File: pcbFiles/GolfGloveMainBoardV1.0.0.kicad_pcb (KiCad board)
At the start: 2 copper layers, 10.5 x 14 mm, 79 parts, among them J1 USB_C_Receptacle, J10 A-1JB, J11 Conn_01x16_Male, J12 HOST_WAKE, J13 TP4, J14 Conn_01x02_Male, J15 Conn_01x02_Male, J2 BT_UART, J3 USB_C_Receptacle, J4 Conn_01x01, J5 Conn_01x01, J6 Conn_01x02_Male, J7 Conn_01x02_Male, J8 Conn_01x02_Male, J9 Conn_01x02_Male, SW1 SW_SPDT, SW2 SW_Push, U1 LSM9DS1TR, U2 LSM9DS1TR, U3 TPS63001DRCT, U4 CYW20719B1KUMLG, U5 MCP73831T-2ACI/OT, U6 XC6119N16A7R-G, Y1 Crystal, Y2 Crystal_GND23

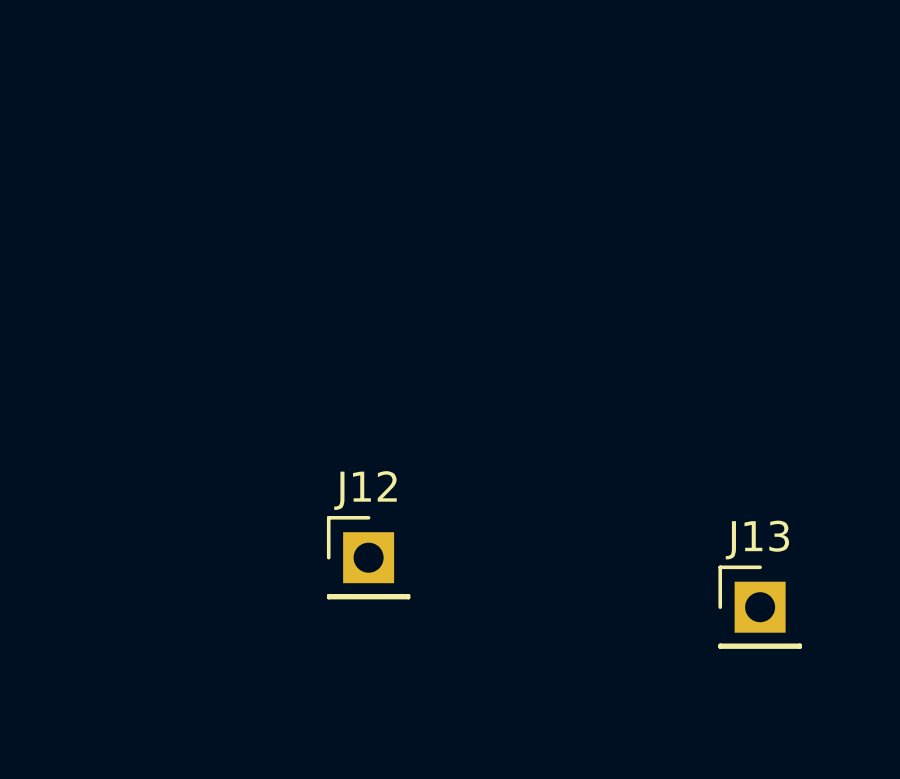
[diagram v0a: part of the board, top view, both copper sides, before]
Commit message: Update Footprints and Board Layers
Still need to get foorprint for x... device and the lpf may need to make them if I cannot find them @willcarroll7
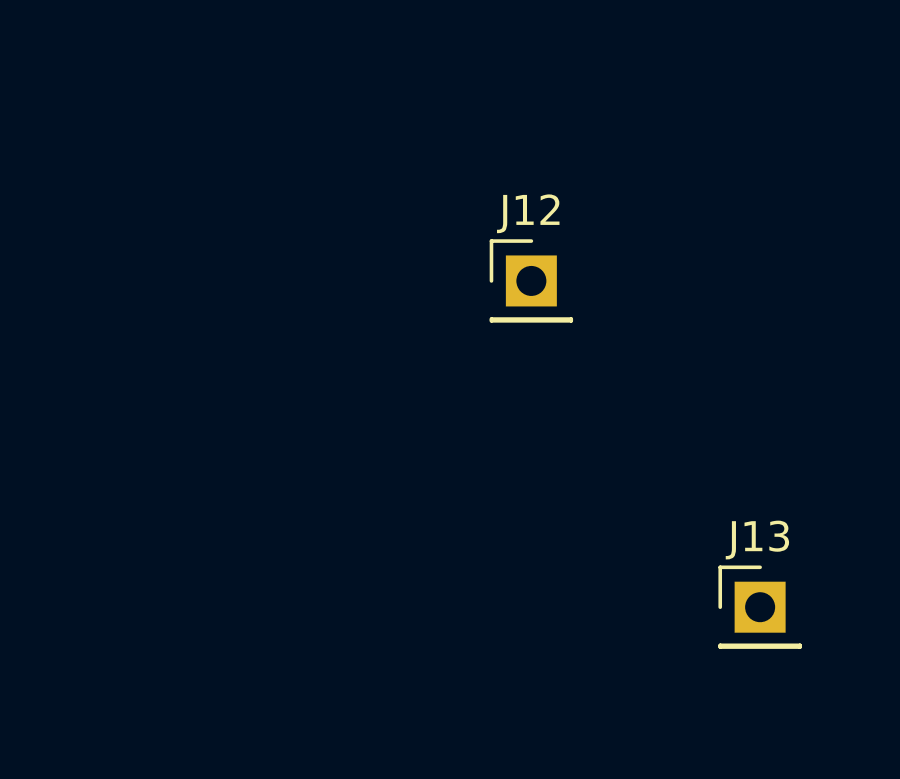
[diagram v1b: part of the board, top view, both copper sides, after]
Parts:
- moved J12 10.7 mm to (168.1, 56.0)
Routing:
- net Net-(J12-Pad1): track 0.00 -> 1.41 mm
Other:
- copper layers 2 -> 4
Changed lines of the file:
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@@
     (thickness 1.6)
     (drawings 11)
-    (tracks 139)
+    (tracks 141)
     (zones 0)
     (modules 79)
@@
   (layers
     (0 F.Cu signal)
+    (1 In1.Cu signal)
+    (2 In2.Cu signal)
     (31 B.Cu signal)
     (32 B.Adhes user)
@@
     (last_trace_width 0.25)
     (trace_clearance 0.15)
-    (zone_clearance 0.508)
+    (zone_clearance 0.25)
     (zone_45_only no)
     (trace_min 0.2)
@@
   )
   (module Pin_Headers:Pin_Header_Straight_1x01_Pitch2.54mm (layer F.Cu)
-    (at 162.7 65.25)
+    (at 168.125 56.025)
     (descr "Through hole straight pin header, 1x01, 2.54mm pitch, single row")
     (tags "Through hole pin header THT 1x01 2.54mm single row")
@@
   (segment (start 68.99 58.365) (end 68.7 58.175) (width 0.25) (layer F.Cu) (net 57))
   (segment (start 71.65 54.125) (end 71.65 53.81) (width 0.25) (layer B.Cu) (net 57))
+  (segment (start 168.125 56.025) (end 168.25 55.9) (width 0.25) (layer B.Cu) (net 88))
+  (segment (start 168.125 56.025) (end 169 55.15) (width 0.25) (layer In1.Cu) (net 88))
 )

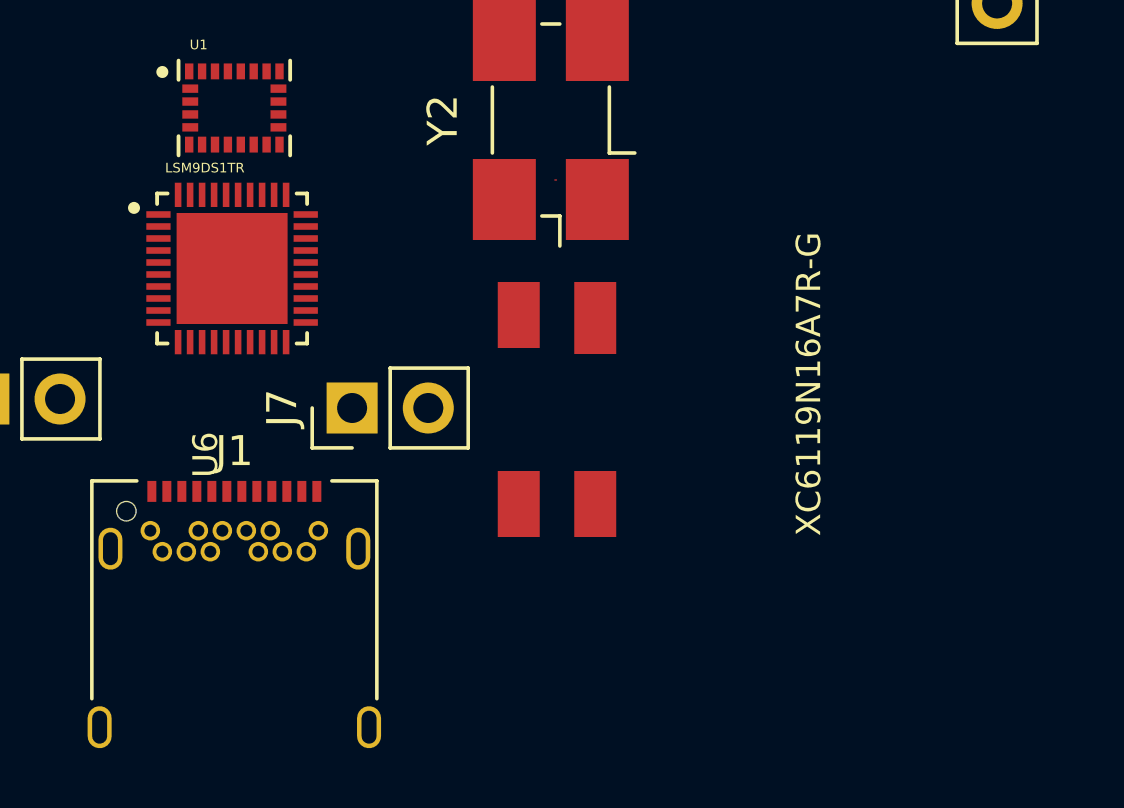
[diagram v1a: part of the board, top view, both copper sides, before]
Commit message: Update the Voltage Detector Footprint
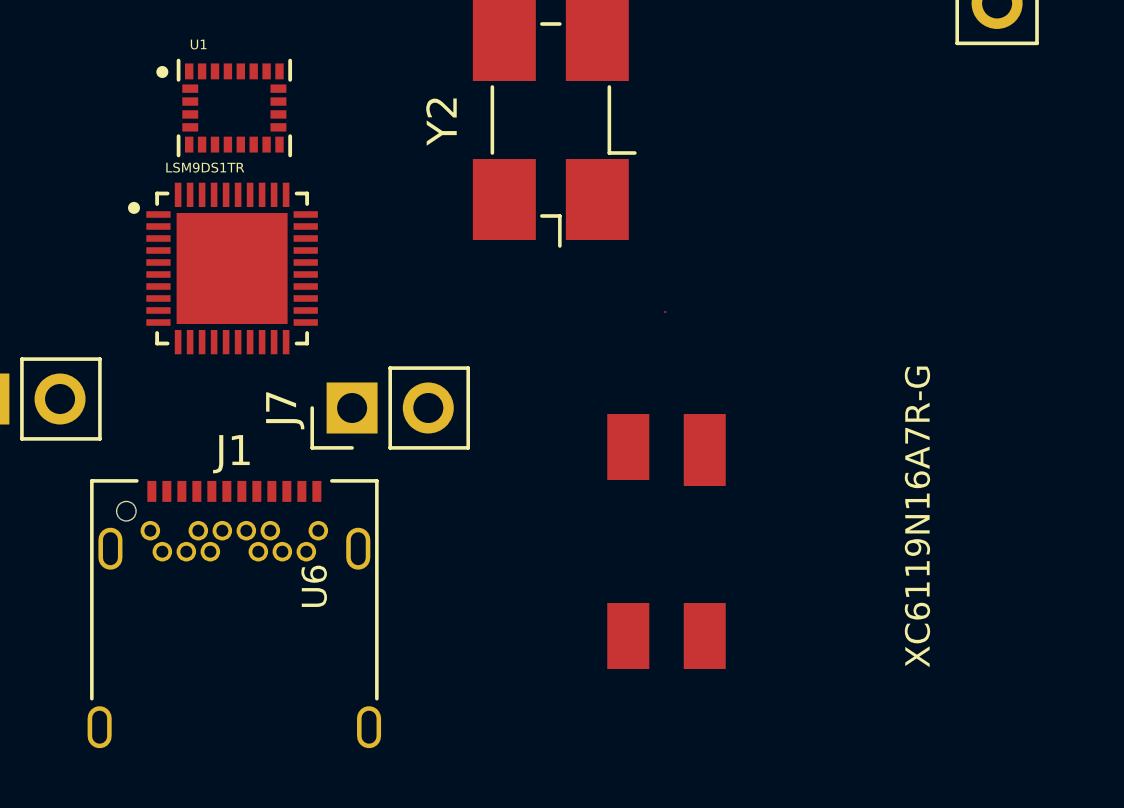
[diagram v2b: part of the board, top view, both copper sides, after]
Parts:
- moved U6 5.72 mm to (68.5, 135.0)
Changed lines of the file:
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@@
   )
   (module AAAA_XC6119_USPN-4:DFN-4 (layer F.Cu)
-    (at 64.85 130.6 90)
+    (at 68.5 135 90)
     (descr "CRYSTAL 24MHZ 18PF SMD")
     (attr smd)

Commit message: Update Circuit With Antenna
This commit will update the pcb with a mock up of the antenna design without the vias, this commit will also update the pressure sensors to be attached to the top of hand unit to allow for USB-C Connection. @willcarroll7
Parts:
- removed C19, C20, C21, C24, C27, C34: C, Capacitors_SMD:C_0402
- removed FL1: EMI_Filter_LCL, Resistors_SMD:R_0603
- removed J10: A-1JB, A-1JB:AMPHENOL_A-1JB
- removed R14: R, Capacitors_SMD:C_0603
- removed U6: XC6119N16A7R-G, AAAA_XC6119_USPN-4:DFN-4
- added AE1: 2450AT42B100E, ANTENNA---------------------:XCVR_2450AT42B100E, F.Cu at (193.4, 101.2)
- added C35: C, Capacitors_SMD:C_0402, F.Cu at (110.2, 93.4)
- added C36, C37: C, Capacitors_SMD:C_0402, F.Cu at (148.5, 105.0)
- added C38: C, Capacitors_SMD:C_0402, F.Cu at (116.4, 103.6)
- added J16: Conn_01x02, Pin_Headers:Pin_Header_Straight_1x02_Pitch2.54mm, F.Cu at (119.6, 110.8)
- added J17: Conn_01x02, Pin_Headers:Pin_Header_Straight_1x02_Pitch2.54mm, F.Cu at (81.2, 94.6)
- added L5: L, Inductors_SMD:L_0603, F.Cu at (154.4, 87.2)
- added L6: L, Inductors_SMD:L_0402, F.Cu at (184.8, 101.2)
- added R15: R, Resistors_SMD:R_0402, F.Cu at (148.5, 105.0)
- added U7: TPS63001DRCT, TPS63001DRCT:SON50P300X300X100-11N, F.Cu at (139.6, 99.2)
- D1: footprint LEDs:LED_0603 -> Capacitors_SMD:C_0603
- J14, J15, J7, J8, J9: value Conn_01x02_Male -> Conn_01x02
- J2: value BT_UART -> Conn_01x06; footprint Socket_Strips:Socket_Strip_Straight_1x04_Pitch2.54mm -> Pin_Headers:Pin_Header_Straight_1x06_Pitch2.54mm
- J6: value Conn_01x02_Male -> Screw_Terminal_01x02
- L1, L2: footprint Inductors_SMD:L_0805 -> Inductors_SMD:L_0402
- R1, R10, R11, R12, R13, R2, R3, R4, R5, R6, R7, R8, R9: footprint Capacitors_SMD:C_0603 -> Resistors_SMD:R_0402
- SW1: footprint SDPT:SDTPSwitchAmazon -> Buttons_Switches_SMD:SW_SPDT_PCM12
- SW2: footprint Buttons_Switches_SMD:SW_SPST_B3S-1000 -> Buttons_Switches_SMD:SW_DIP_x1_W8.61mm_Slide_LowProfile
- U1: value LSM9DS1TR -> MCP73831T-2ACI/OT; footprint LSM9DS1TR:PQFN43P300X350X102-24N -> MCP73831T-2ACI_OT:SOT95P280X145-5N
- U2: value LSM9DS1TR -> XC6119N16A7R-G; footprint PQFN43P300X350X102-24N -> DFN-4-------------------------:DFN-4
- U3: value TPS63001DRCT -> LSM9DS1TR; footprint SON50P300X300X100-11N -> LSM9DS1TR:PQFN43P300X350X102-24N
- U4: footprint QFN40P500X500X60-41N -> CYW20719B1KUMLG:QFN40P500X500X60-41N
- U5: value MCP73831T-2ACI/OT -> LSM9DS1TR; footprint MCP73831T-2ACI_OT:SOT95P280X145-5N -> LSM9DS1TR:PQFN43P300X350X102-24N
- moved L1 157.3 mm to (186.0, 102.0)
- moved J14 132.3 mm to (166.6, 127.4)
- moved R1 127.9 mm to (148.5, 105.0)
- moved R2 127.4 mm to (148.5, 105.0)
- moved R3 127.0 mm to (148.5, 105.0)
- moved R4 126.6 mm to (148.5, 105.0)
- moved R5 126.1 mm to (148.5, 105.0)
- moved R6 125.7 mm to (148.5, 105.0)
- moved R7 125.3 mm to (148.5, 105.0)
- moved R8 125.0 mm to (148.5, 105.0)
- moved U5 124.7 mm to (158.4, 92.8)
- moved R9 124.6 mm to (148.5, 105.0)
- moved R10 124.3 mm to (148.5, 105.0)
- moved R11 124.0 mm to (148.5, 105.0)
- moved R12 123.7 mm to (148.5, 105.0)
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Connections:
- net Net-(J2-Pad2) renamed /BT_UART_RTS
- net Net-(J2-Pad4) renamed /BT_UART_RX
- net PSensor2 renamed Net-(J11-Pad16)
- C1 pad 1: BatteryOutBuck -> ChgVDD
- C10 pad 1: 3.3v -> GND
- C10 pad 2: GND -> Net-(C10-Pad2)
- C12 pad 1: ChgVDD -> GND
- C12 pad 2: GND -> 3.3v
- C15 pad 1: BatteryOutChg -> 3.3v
- C16 pad 1: USBGND -> GND
- C16 pad 2: USBVCC -> Net-(C16-Pad2)
- C17 pad 1: USBVCC -> GND
- C17 pad 2: USBGND -> Net-(C17-Pad2)
- C18 pad 1: USBGND -> 3.3v
- C18 pad 2: USBVCC -> GND
- C2 pad 1: Net-(C2-Pad1) -> BatteryOutChg
- C3 pad 1: GND -> Net-(C3-Pad1)
- C3 pad 2: 3.3v -> GND
- C4 pad 1: 3.3v -> GND
- C4 pad 2: GND -> Net-(C4-Pad2)
- C6 pad 1: GND -> 3.3v
- C6 pad 2: Net-(C6-Pad2) -> GND
- J11 pad 1: Sensor1 -> PSensor1
- J11 pad 12: Sensor3 -> PSensor1
- J11 pad 2: Sensor2 -> PSensor1
- J11 pad 8: Sensor4 -> PSensor1
- J11 pad 9: PSensor1 -> Net-(J11-Pad9)
- J14 pad 1: 3.3v -> PSensor1
- J14 pad 2: PSensor1 -> 3.3v
- J15 pad 1: 3.3v -> PSensor1
- J15 pad 2: PSensor1 -> 3.3v
- J2 pad 1: Net-(J2-Pad1) -> GND
- J2 pad 3: Net-(J2-Pad3) -> Net-(J17-Pad2)
- J3 pad A1: USBGND -> GND
- J3 pad A10: Net-(J3-PadA10) -> PSensor1
- J3 pad A11: Net-(J3-PadA11) -> PSensor1
- J3 pad A12: USBGND -> GND
- J3 pad A2: USBVCC -> 3.3v
- J3 pad A3: USBVCC -> 3.3v
- J3 pad A6: SCLK-USB -> SCLK
- J3 pad A7: SDA-USB -> SDA
- J3 pad B1: USBGND -> GND
- J3 pad B10: Net-(J3-PadB10) -> PSensor1
- J3 pad B11: Net-(J3-PadB11) -> PSensor1
- J3 pad B12: USBGND -> GND
- J3 pad B2: USBVCC -> 3.3v
- J3 pad B3: USBVCC -> 3.3v
- J3 pad B6: SCLK-USB -> SCLK
- J3 pad B7: SDA-USB -> SDA
- J3 pad S1: USBGND -> GND
- J6 pad 1: 3.3v -> GND
- J6 pad 2: Sensor1 -> Net-(C4-Pad2)
- J7 pad 1: 3.3v -> PSensor1
- J7 pad 2: Sensor2 -> 3.3v
- J8 pad 1: 3.3v -> PSensor1
- J8 pad 2: Sensor3 -> 3.3v
- J9 pad 1: 3.3v -> PSensor1
- J9 pad 2: Sensor4 -> 3.3v
- L1 pad 2: Net-(L1-Pad2) -> Net-(AE1-Pad1)
- R1 pad 1: 3.3v -> Net-(R1-Pad1)
- R1 pad 2: SCLK -> GND
- R10 pad 2: Sensor4 -> PSensor1
- R12 pad 1: 3.3v -> GND
- R12 pad 2: Net-(C34-Pad2) -> PSensor1
- R2 pad 1: 3.3v -> Net-(D1-Pad2)
- R2 pad 2: SDA -> ChgVDD
- R3 pad 1: BatteryOutBuck -> 3.3v
- R3 pad 2: Net-(C2-Pad1) -> Net-(C4-Pad2)
- R5 pad 1: Net-(R5-Pad1) -> SCLK
- R5 pad 2: GND -> 3.3v
- R6 pad 1: Net-(D1-Pad2) -> SDA
- R6 pad 2: ChgVDD -> 3.3v
- R7 pad 2: Sensor1 -> PSensor1
- R8 pad 2: Sensor2 -> PSensor1
- R9 pad 2: Sensor3 -> PSensor1
- SW2 pad 2: Net-(C34-Pad2) -> Net-(C4-Pad2)
- U1 pad 1: 3.3v -> Net-(D1-Pad1)
- U1 pad 2: SCLK -> GND
- U1 pad 3: 3.3v -> BatteryOutChg
- U1 pad 4: SDA -> ChgVDD
- U1 pad 5: Net-(U1-Pad5) -> Net-(R1-Pad1)
- U2 pad 1: USBVCC -> RST_N
- U2 pad 2: SCLK-USB -> Net-(C3-Pad1)
- U2 pad 3: USBVCC -> GND
- U2 pad 4: SDA-USB -> Net-(C4-Pad2)
- U3 pad 10: 3.3v -> Net-(U3-Pad10)
- U3 pad 11: GND -> Net-(U3-Pad11)
- U3 pad 2: Net-(L1-Pad2) -> SCLK
- U3 pad 3: GND -> 3.3v
- U3 pad 4: Net-(L1-Pad1) -> SDA
- U3 pad 5: BatteryOutBuck -> Net-(U3-Pad5)
- U3 pad 6: Net-(C2-Pad1) -> Net-(U3-Pad6)
- U3 pad 7: Net-(C2-Pad1) -> Net-(U3-Pad7)
- U3 pad 8: Net-(C2-Pad1) -> Net-(U3-Pad8)
- U3 pad 9: GND -> Net-(U3-Pad9)
- U4 pad 1: Sensor3 -> PSensor1
- U4 pad 18: Net-(C24-Pad1) -> Net-(L1-Pad1)
- U4 pad 28: Net-(J2-Pad3) -> /BT_UART_TX
- U4 pad 3: Sensor1 -> PSensor1
- U4 pad 30: Net-(J2-Pad1) -> /BT_UART_CTS
- U4 pad 33: Sensor4 -> PSensor1
- U4 pad 38: PSensor1 -> Net-(J11-Pad9)
- U4 pad 4: Sensor2 -> PSensor1
- U5 pad 1: Net-(D1-Pad1) -> 3.3v
- U5 pad 2: GND -> SCLK
- U5 pad 3: BatteryOutChg -> 3.3v
- U5 pad 4: ChgVDD -> SDA
- U5 pad 5: Net-(R5-Pad1) -> Net-(U5-Pad5)
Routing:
- net USBGND: track 44.8 -> 0.00 mm, vias 1 -> 0
- net USBVCC: track 34.1 -> 0.00 mm, vias 4 -> 0
- net SDA-USB: track 11.4 -> 0.00 mm, vias 1 -> 0
- net Net-(L1-Pad1): track 0.00 -> 9.50 mm
- net SCLK-USB: track 7.33 -> 0.00 mm, vias 2 -> 0
- net Net-(C19-Pad2): track 4.50 -> 0.00 mm, vias 2 -> 0
- net Net-(AE1-Pad1): track 0.00 -> 4.35 mm
- net Net-(C20-Pad2): track 4.23 -> 0.00 mm, vias 2 -> 0
- net Net-(J12-Pad1): track 1.41 -> 0.00 mm
- added copper zone on F.Cu, net GND
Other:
- board outline removed
- net class Antenna added: clearance 0.2, trace_width 0.29337, via_dia 0.6, via_drill 0.4
- board text removed: "C16"
- board text removed: "C17"
- board text removed: "C18"
- board text removed: "C19"
- board text removed: "C20"
